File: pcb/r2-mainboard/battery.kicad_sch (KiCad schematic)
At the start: 0 parts

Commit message: R2: capture battery.kicad_sch -- charger, power path, gauge, USB-C
First real sheet of the R2 schematic. ERC reports 16 violations, all of them
'the rest of the board does not exist yet' (12 unconnected sheet pins on the
parent, 4 on CHG_QON# which the MCU and power button drive). No electrical or
structural errors. Netlist exported and read back node by node.

tools/schgen.py is a small KiCad schematic writer built on the kicad-happy
sexp parser: it loads symbol geometry from .kicad_sym, computes absolute pin
coordinates through the placement transform, and emits KiCad 9 format that
'kicad-cli sch upgrade' normalises to KiCad 10. Used once per sheet -- after
a sheet is opened in Eeschema the .kicad_sch is the source of truth.

r2.kicad_sym holds the three symbols KiCad's libraries do not: BQ25892RTW
(derived from the stock BQ25895RTW by renaming pins 2, 3 and 24), MAX17048,
and a flattened USBLC6-2SC6 -- flattened because embedding KiCad's derived
form makes ERC report lib_symbol_mismatch.

Reading the finished netlist found three omissions, now fixed: CE had no
defined level (datasheet requires it be driven, and low enables charging so a
flat cell can recover), OTG could float into boost mode, and the gauge's
open-drain ALRT had no pull-up.

Co-Authored-By: Claude Opus 5 <noreply@anthropic.com>
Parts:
- added C1: 1uF/25V, Capacitor_SMD:C_0402_1005Metric, symbol Device:C
- added C2: 8.2uF/25V, Capacitor_SMD:C_0805_2012Metric, symbol Device:C
- added C3: 47nF/25V, Capacitor_SMD:C_0402_1005Metric, symbol Device:C
- added C4, C5, C7: 10uF/10V, Capacitor_SMD:C_0805_2012Metric, symbol Device:C
- added C6: 4.7uF/10V, Capacitor_SMD:C_0805_2012Metric, symbol Device:C
- added C8: 100nF/16V, Capacitor_SMD:C_0402_1005Metric, symbol Device:C
- added F1: 1.5A hold, Resistor_SMD:R_1206_3216Metric, symbol Device:Polyfuse
- added J1: USB-C 16P, Connector_USB:USB_C_Receptacle_HRO_TYPE-C-31-M-12, symbol Connector:USB_C_Receptacle_USB2.0_16P
- added J2: JST-PH 3P, Connector_JST:JST_PH_B3B-PH-K_1x03_P2.00mm_Vertical, symbol Connector_Generic:Conn_01x03
- added L1: 1uH/3A, Inductor_SMD:L_Taiyo-Yuden_NR-30xx, symbol Device:L
- added R1, R2: 5.1k, Resistor_SMD:R_0402_1005Metric, symbol Device:R
- added R10: 30.1k/1%, Resistor_SMD:R_0402_1005Metric, symbol Device:R
- added R11, R14, R15: 0R, Resistor_SMD:R_0402_1005Metric, symbol Device:R
- added R12, R13: 100k/1%, Resistor_SMD:R_0402_1005Metric, symbol Device:R
- added R16, R19, R3, R4, R5, R6, R7: 10k, Resistor_SMD:R_0402_1005Metric, symbol Device:R
- added R17, R18: 100k, Resistor_SMD:R_0402_1005Metric, symbol Device:R
- added R8: 260R/1%, Resistor_SMD:R_0402_1005Metric, symbol Device:R
- added R9: 5.23k/1%, Resistor_SMD:R_0402_1005Metric, symbol Device:R
- added U1: BQ25892RTW, Package_DFN_QFN:WQFN-24-1EP_4x4mm_P0.5mm_EP2.6x2.6mm, symbol r2:BQ25892RTW
- added U2: MAX17048G+T10, Package_DFN_QFN:TDFN-8-1EP_2x2mm_P0.5mm_EP0.8x1.2mm, symbol r2:MAX17048
- added U3: USBLC6-2SC6, Package_TO_SOT_SMD:SOT-23-6, symbol r2:USBLC6-2SC6
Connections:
- new net: F1.1, J1.A4 (VBUS), J1.A9 (VBUS), J1.B4 (VBUS), J1.B9 (VBUS)
- new net: R8.1, U1.10 (ILIM)
- new net: C3.2, L1.1, U1.19 (SW), U1.20 (SW)
- new net: C3.1, U1.21 (BTST)
- new net: C2.2, U1.23 (PMID)
- new net: J1.A7 (D-), J1.B7 (D-), U3.1 (I/O1)
- new net: J1.A6 (D+), J1.B6 (D+), U3.3 (I/O2)
- new net +3V3_AON: R16.2, R19.1, R3.1, R4.1, R5.1, R6.1, R7.1
- new net +VBAT: C7.1, C8.1, J2.1 (Pin_1), U1.13 (BAT), U1.14 (BAT), U2.3 (VDD)
- new net +VBUS: C1.1, F1.2, R12.1, U1.1 (VBUS), U3.5 (VBUS)
- new net +VSYS: C4.1, C5.1, L1.2, U1.15 (SYS), U1.16 (SYS)
- new net CHG_CE#: R17.1, U1.9 (~{CE})
- new net CHG_DSEL: R16.1, U1.24 (NC/DSEL)
- new net CHG_INT#: R5.2, U1.7 (~{INT})
- new net CHG_OTG: R18.1, U1.8 (OTG)
- new net CHG_PG#: R15.1, R3.2, U1.3 (~{PG})
- new net CHG_PSEL: R11.1, R14.1, U1.2 (PSEL)
- new net CHG_QON#: U1.12 (~{QON})
- new net CHG_STAT#: R4.2, U1.4 (STAT)
- new net CHG_TS: J2.2 (Pin_2), R10.1, R9.2, U1.11 (TS)
- new net GAUGE_ALRT#: R19.2, U2.5 (~{ALRT})
- new net GND: C1.2, C2.1, C4.2, C5.2, C6.2, C7.2, C8.2, J1.A1 (GND), J1.A12 (GND), J1.B1 (GND), J1.B12 (GND), J1.SH (SHIELD), J2.3 (Pin_3), R1.2, R10.2, R11.2, R13.2, R17.2, R18.2, R2.2, R8.2, U1.17 (PGND), U1.18 (PGND), U1.25 (PGND), U2.1 (CTG), U2.4 (GND), U2.6 (QSTRT), U2.9 (EP), U3.2 (GND)
- new net REGN: C6.1, R9.1, U1.22 (REGN)
- new net SCL_AON: R7.2, U1.5 (SCL), U2.7 (SCL)
- new net SDA_AON: R6.2, U1.6 (SDA), U2.8 (SDA)
- new net USB_CC1: J1.A5 (CC1), R1.1
- new net USB_CC2: J1.B5 (CC2), R2.1
- new net USB_DM: R15.2, U3.6 (I/O1)
- new net USB_DP: R14.2, U3.4 (I/O2)
- new net VBUS_DET: R12.2, R13.1
- no-connect marks 0 -> 3
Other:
- note added: "1S cell, 5000 mAh, with pack NTC"
- note added: "Charger with power path — BQ25892"
- note added: "Defaults while the MCU is unpowered: charging enabled, boost off"
- note added: "ERC power flags — drop the +3V3_AON flag once"
- note added: "Fuel gauge — MAX17048, I2C 0x36"
- note added: "No NTC in pack -> fit 7.68k/10k instead."
- note added: "PSEL low = adapter source"
- note added: "Pull-ups to +3V3_AON (always-on domain)"
- note added: "Second-source option field — fit ONLY for the BQ25890/95 (D+/D-/DSEL variant). Not fitted for the BQ25892/96."
- note added: "TS: 103AT NTC in the pack. RT1/RT2 solved from"
- note added: "USB-C sink: 5.1k Rd on each CC, separately"
- note added: "USB-C — charge input and USB2 device port"
- note added: "V(T1) 73.25% and V(T5) 34.375% of REGN."
- note added: "VBUS presence, 2.5 V at 5 V in"
- note added: "power.kicad_sch sources that rail."
- note added: "to other sheets"

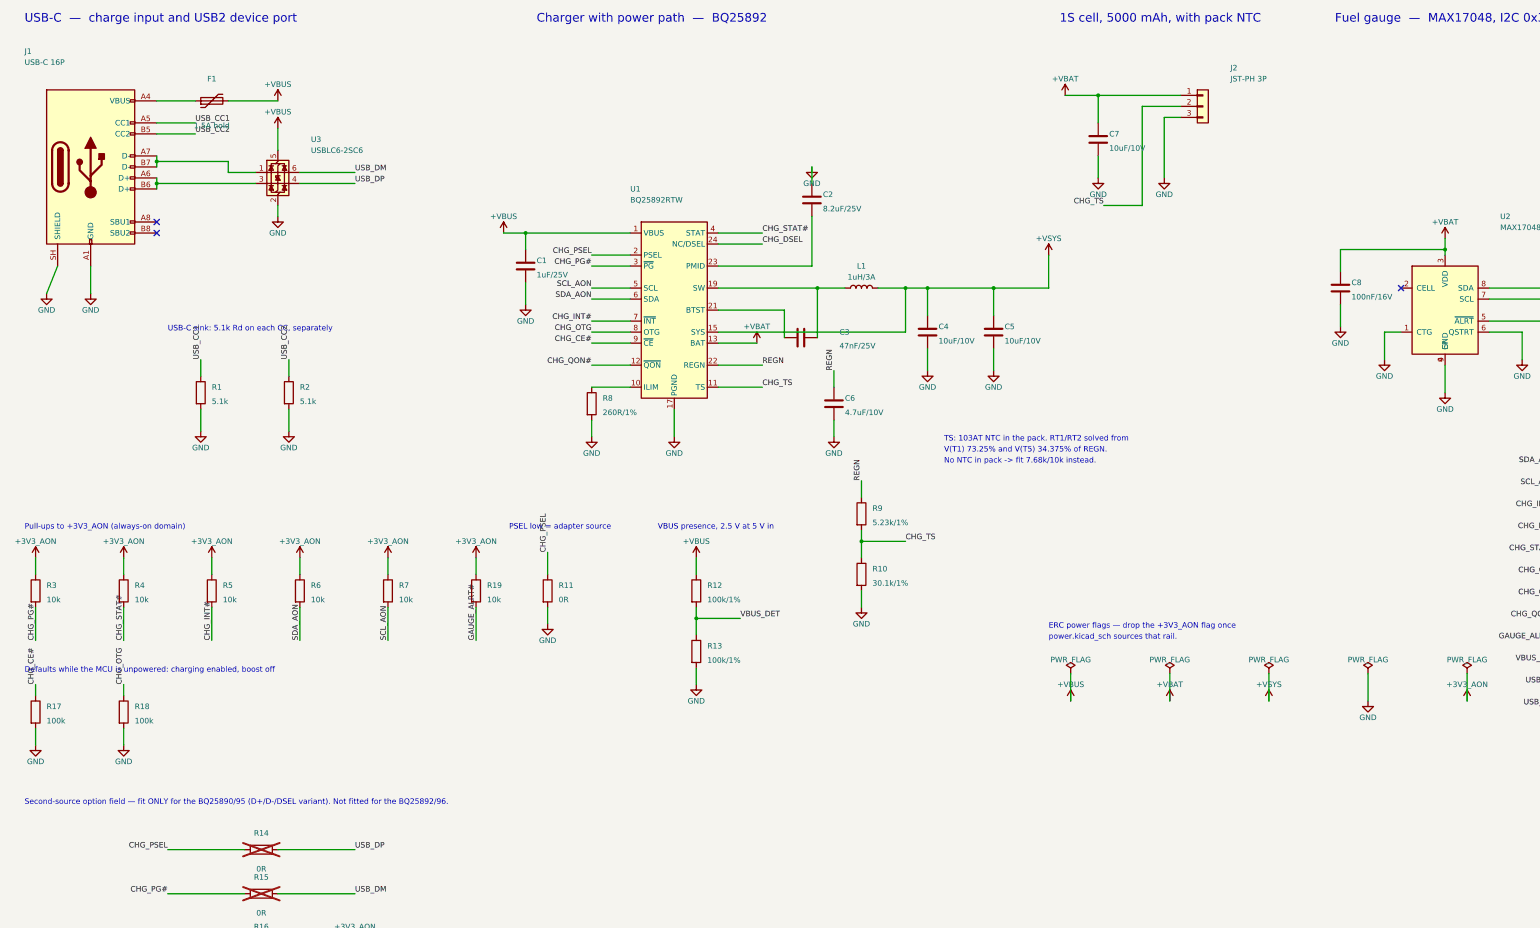
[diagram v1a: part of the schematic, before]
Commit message: R2: battery sheet review pass 1, plus notes and parts scratch
Rework battery.kicad_sch and its spec after the first review round, and
carry the follow-on touch-ups into the other R2 sheets. Adds the
Analyse_battery.md review write-up, the patch_battery_review1.py script
that applied it, and a parts/ scratch list.

Co-Authored-By: Claude Opus 5 <noreply@anthropic.com>
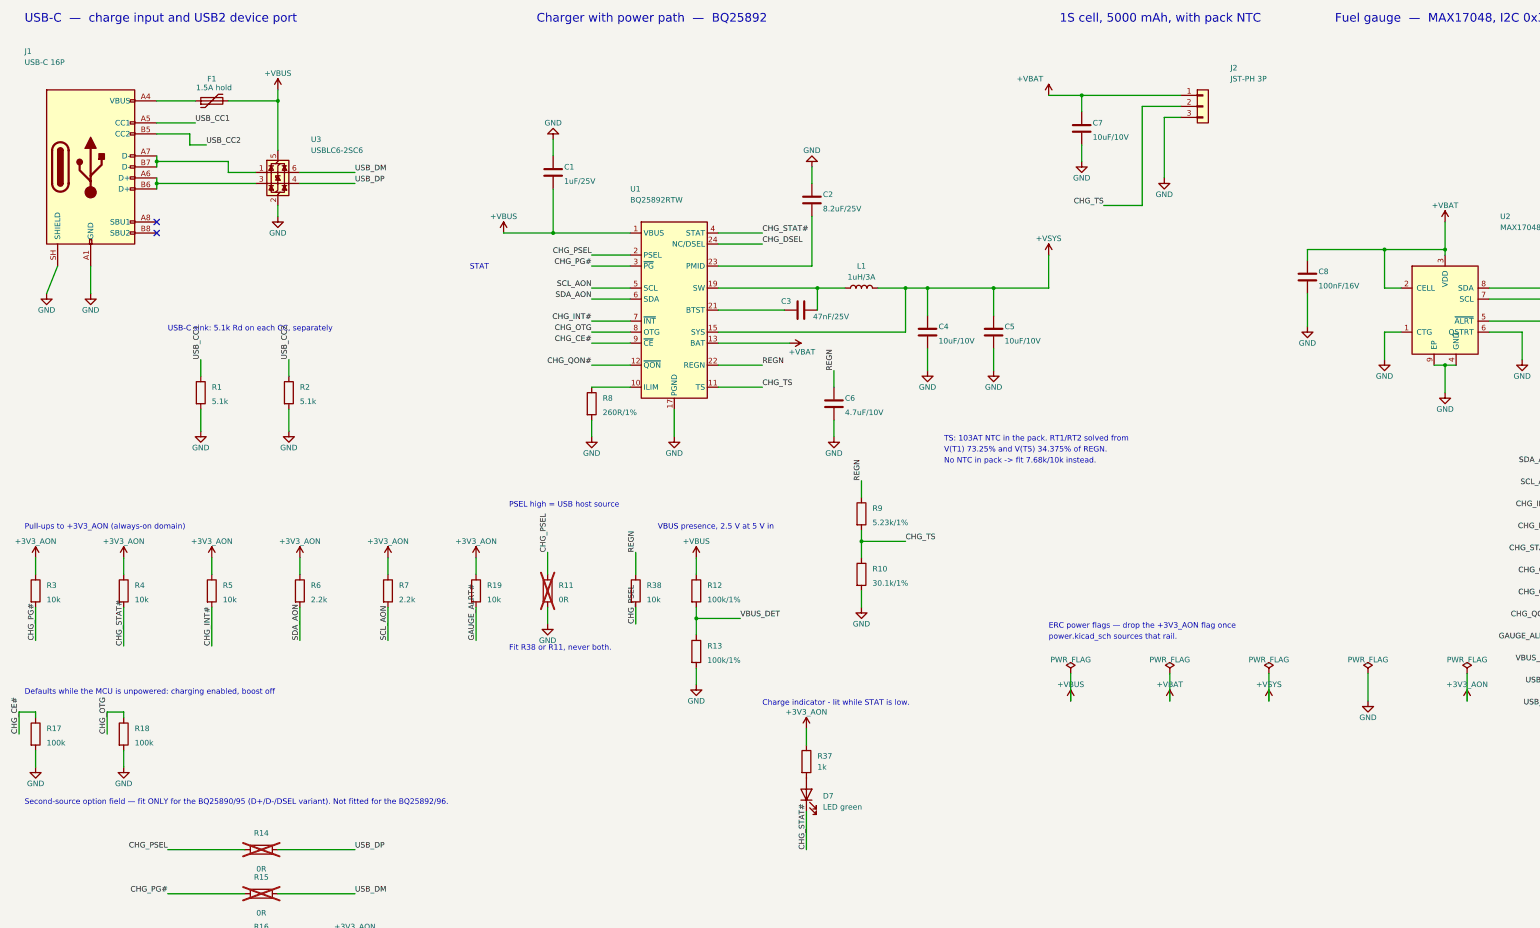
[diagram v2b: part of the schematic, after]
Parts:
- added D7: LED green, LED_SMD:LED_0603_1608Metric, symbol Device:LED
- added R37: 1k, Resistor_SMD:R_0402_1005Metric, symbol Device:R
- added R38: 10k, Resistor_SMD:R_0402_1005Metric, symbol Device:R
- R11: now not fitted
- R6, R7: value 10k -> 2.2k
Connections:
- net +3V3_AON: now also R37.1
- net +VBAT: now also U2.2 (CELL)
- net +VBUS: now also C1.2; no longer C1.1
- net CHG_PSEL: now also R38.2
- net CHG_STAT#: now also D7.1 (K)
- net GND: now also C1.1; no longer C1.2
- net REGN: now also R38.1
- new net: D7.2 (A), R37.2
- no-connect marks 3 -> 2
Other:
- note added: "Charge indicator - lit while STAT is low."
- note added: "Fit R38 or R11, never both."
- note added: "PSEL high = USB host source"
- note added: "STAT"
- note removed: "PSEL low = adapter source"
- moved on the sheet: C1, C3, C7, C8, R17, R18

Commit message: R2: cell attaches two ways -- Pico-Lock, or pads soldered straight to the board
J2 becomes a Molex Pico-Lock 504050-0391: 1.5 mm pitch, 3 circuits, right-angle
SMT, 3.5 A per contact against ~2 A of charge current, and 2.00 mm mated against
the JST-PH's ~6.0. Right-angle on purpose -- the leads then exit parallel to the
board instead of standing up, and thickness is what this device is short of once
the cell's 7.0 mm and the SoM's 5 mm are counted. Pico-EZmate, which battery.md
§10.9 had suggested, is rejected as too niche a family; Pico-Lock carries more
current for 0.15 mm more height.

J25 is new: three bare copper pads on the same three nets, for soldering the
cell's leads directly. Not an either/or -- same nets, fit either or both. No
paste, because a stencil aperture over a 6 mm^2 pad leaves a bump under the
wire, and +/T/- silk markers because the connector's polarisation does not
protect these and reversing a 5 Ah pack is not a small mistake.

What does not go away: the PL706090 ships with a JST 1.25 mm plug rated 1 A, so
the pack must be re-terminated whichever attachment is used. A phone-style
board-to-board connector -- the literal reading of "clips on like a smartphone"
-- cannot work here at all: in a phone the battery carries an FPC with a BTB
plug and the receptacle parallels several fine-pitch contacts per rail, and this
pack has flying leads. Pico-Lock's positive lock gives the click-in retention
without needing a custom flex built onto the cell.

battery.kicad_sch is a reviewed sheet, so this is a surgical patch that refuses
to run twice, not a regeneration. The Pico-Lock footprint already ships with
KiCad 10; the pad footprint is generated.

Verified: J2 and J25 land pin-for-pin on +VBAT, /battery/CHG_TS and GND with no
stray connections, the NTC pad reaching the R9/R10 divider midpoint; ERC
unchanged at 33 non-footprint violations; check_ucf 0 failures; rendered and
read -- the first attempt printed its note straight through the existing TS note
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
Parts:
- added J25: SolderPads 3x, r2:SolderPads_1x03_P3.50mm_Wire, symbol Connector_Generic:Conn_01x03
- J2: value JST-PH 3P -> Pico-Lock 504050-0391; footprint Connector_JST:JST_PH_B3B-PH-K_1x03_P2.00mm_Vertical -> Connector_Molex:Molex_Pico-Lock_504050-0391_1x03-1MP_P1.50mm_Horizontal
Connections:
- net +VBAT: now also J25.1 (Pin_1)
- net CHG_TS: now also J25.2 (Pin_2)
- net GND: now also J25.3 (Pin_3)
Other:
- note added: "*** The PL706090 ships with a JST 1.25 mm plug rated 1 A against ~2 A of"
- note added: "*** charge current, so the pack must be re-terminated. battery.md §9.1."
- note added: "Cell attachment -- J2 or J25, same three nets, fit either or both."
- note added: "J2 Pico-Lock 504050-0391: 3.5 A/contact, 2.00 mm mated, positive lock,"
- note added: "J25 bare copper pads, for soldering the cell's leads directly."
- note added: "right-angle. Replaces a JST-PH that was 2 A and ~6.0 mm tall."

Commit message: R2: MPNs into the schematic -- and five caps carry the wrong part number
Sourcing data lived in docs/*.md, not in the schematic, so the BOM the
fab would read had 3 of 96 lines with an MPN. Resolved every LCSC code
already on the board against LCSC's own catalogue and wrote MPN +
Manufacturer back: 53 -> 60 lines, 218 components. Added LCSC codes for
L10-L13, U42 and J22/J23 from the per-sheet docs.

Verified before writing: 321 refs and 519 nets identical before and
after, no duplicated properties, pre-existing MPNs untouched.

Cross-checking each passive value against the part its LCSC code
actually names found five wrong ones, all of them the ADC sense-divider
filter caps on power_mon:

  C91                 1nF/50V  carries C131394  = 100 nF
  C163 C164 C168 C169 1nF/25V  carries C6119801 = 470 nF

Left unwritten rather than cementing the error. C1523 (0402B102K500NT,
1 nF 50 V X7R 0402, JLC Basic, 5.3 M stock) covers both positions.

Also held back: U41, whose C39313 is XC6SLX16-**2**FTG256C while
fpga.md specifies the -3 speed grade.

frontlight.md cites C1848394 as the FPC connector on J22/J23; that code
is TPS22914BYFPR. The 6-pin sibling of J24's C5213749 is C5213748.

Co-Authored-By: Claude Opus 5 <noreply@anthropic.com>
Claude-Session: https://claude.ai/code/session_01MnesETWABbVdbcVnCKfKVs
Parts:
- J1: Manufacturer (none) -> Korean Hroparts Elec
- U1: Manufacturer (none) -> TI
- U2: Manufacturer (none) -> MAXIM
- U3: MPN (none) -> USBLC6-2SC6; Manufacturer (none) -> ST
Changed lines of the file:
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@@
 			)
 		)
+		(property "Manufacturer" "MAXIM" (at 0 0 0)
+			(effects
+				(font
+					(size 1.27 1.27)
+				)
+				(hide yes)
+			)
+		)
 		(pin "1"
 		)
@@
 			)
 		)
+		(property "Manufacturer" "TI" (at 0 0 0)
+			(effects
+				(font
+					(size 1.27 1.27)
+				)
+				(hide yes)
+			)
+		)
 		(pin "2"
 		)
@@
 			)
 		)
+		(property "Manufacturer" "ST" (at 0 0 0)
+			(effects
+				(font
+					(size 1.27 1.27)
+				)
+				(hide yes)
+			)
+		)
+		(property "MPN" "USBLC6-2SC6" (at 0 0 0)
+			(effects
+				(font
+					(size 1.27 1.27)
+				)
+				(hide yes)
+			)
+		)
 		(pin "5"
 		)
@@
 			)
 		)
+		(property "Manufacturer" "Korean Hroparts Elec" (at 0 0 0)
+			(effects
+				(font
+					(size 1.27 1.27)
+				)
+				(hide yes)
+			)
+		)
